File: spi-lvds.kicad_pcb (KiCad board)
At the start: 2 copper layers, 39.9 x 34.9 mm, 8 parts

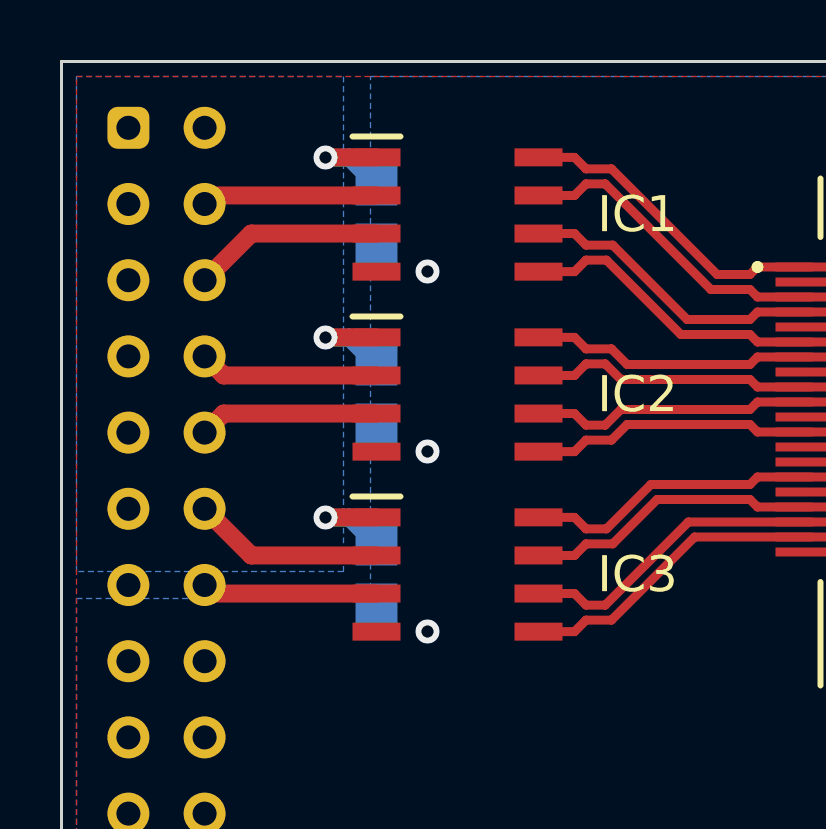
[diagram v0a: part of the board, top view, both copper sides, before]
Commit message: increase via size
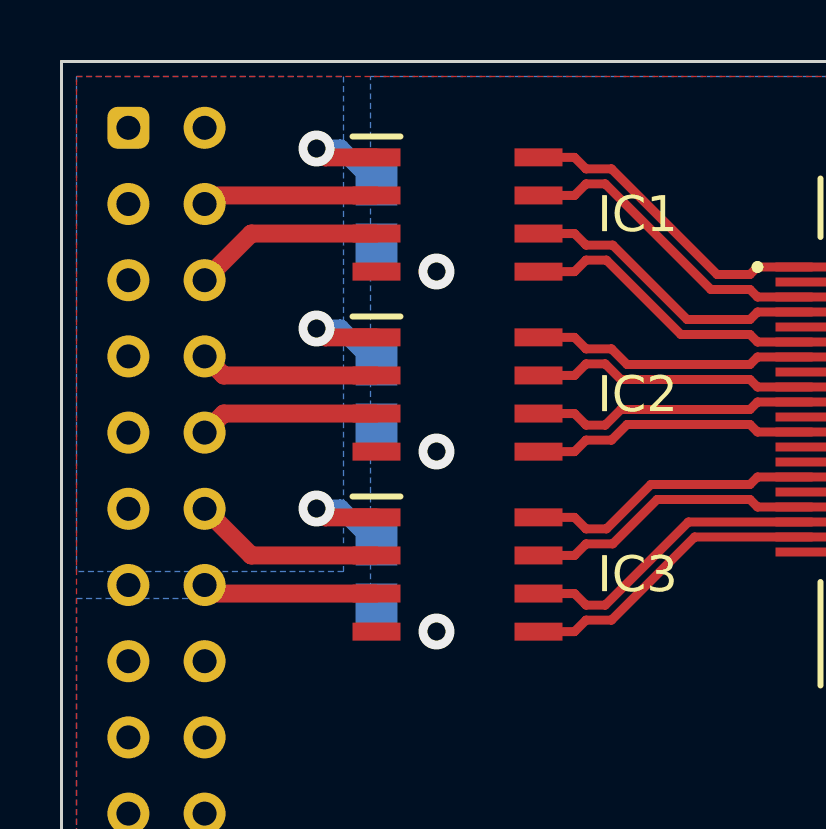
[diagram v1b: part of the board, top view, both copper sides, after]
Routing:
- net VCC: track 11.3 -> 13.9 mm

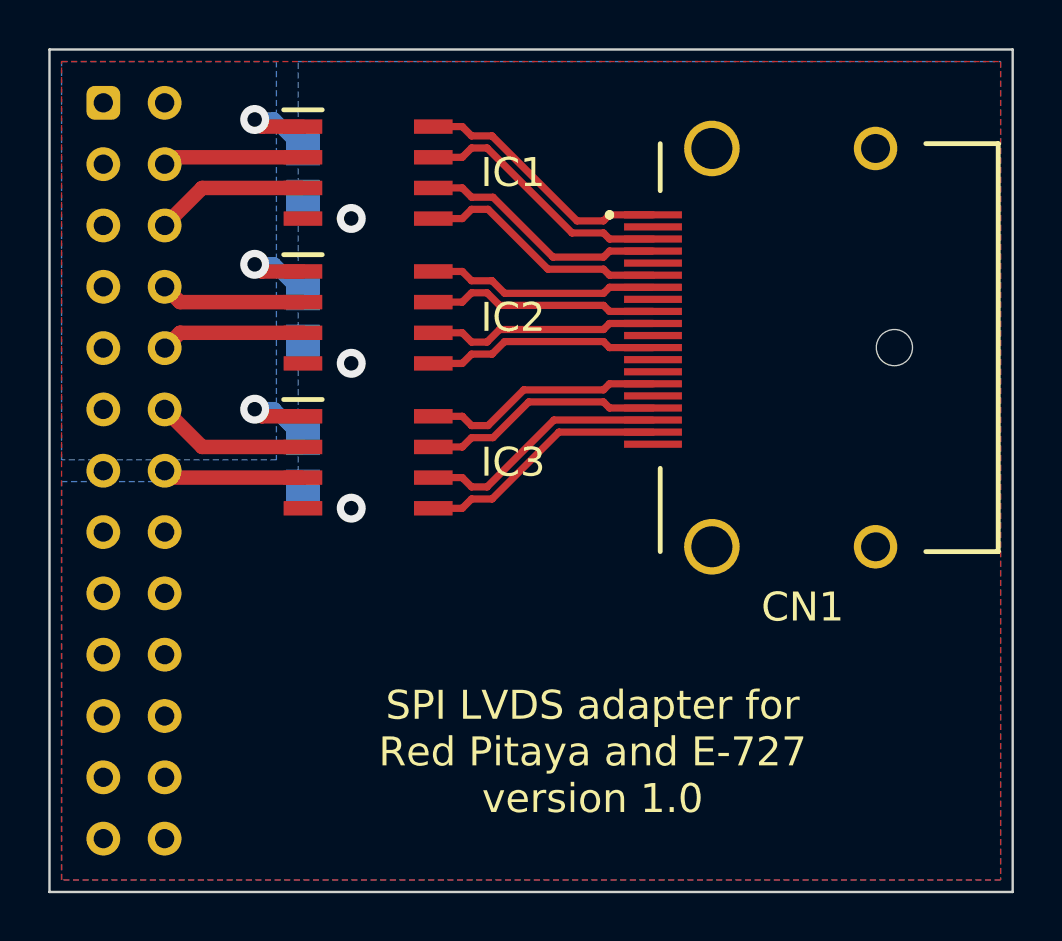
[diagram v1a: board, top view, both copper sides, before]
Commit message: add gnd traces
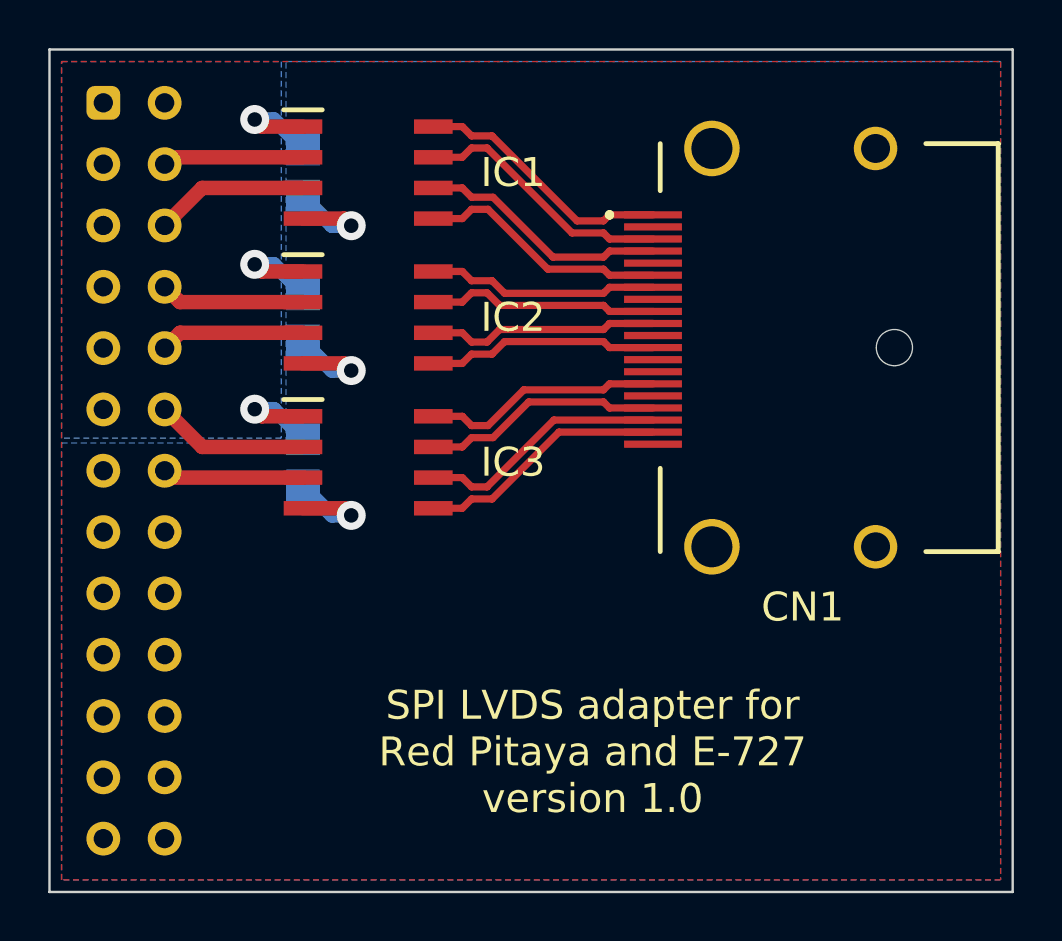
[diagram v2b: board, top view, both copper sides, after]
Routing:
- net GND: track 0.01 -> 13.9 mm
- added copper zone on B.Cu, net (none)
- removed copper zone on B.Cu, net GND

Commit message: improve GND and VCC
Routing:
- net VCC: track 13.9 -> 13.1 mm
- added copper zone on B.Cu, net GND
- removed copper zone on B.Cu, net (none)
